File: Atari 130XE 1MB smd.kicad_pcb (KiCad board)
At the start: 2 copper layers, 324 x 204 mm, 366 parts, among them J1 SIO, J10 Mem_on_off, J102 pin, J103 pin, J2 Video, J201 Diagnostic, J202 Diag, J210 Diag, J24 Cartridge, J4 Expansion, J5 Joystick_Port, J50 Test_signal, J500 Basic_sel, J501 TPP_sel, J51 To_GND, J6 Joystick_Port, J7 Power, J8 Keyboard, Q1 2N3904, Q10 PN2222A, Q101 BC849, Q11 PN2222A, Q2 2N3904, Q3 2N3904, Q4 2N3906, Q6 2N3904, SW1 Switch_power_on, U10 DRAM_4464, U100 74LS157, U101 74LS74, U102 74HC02, U103 74HC02, U104 74LS157, U105 74HC74, U17 GTIA, U18 74LS08, U19 LM555, U2 74LS138, U20 4050, U21 74LS74, U22 POKEY, U23 PIA, U24 CD4051B, U25 CD4051B, U3 MMU, U4 27C010, U40 GAL20V8_DIP, U41 74LS157, U42 74LS175, U43 DRAM_1MB_4bit, U44 DRAM_1MB_4bit, U5 27C010, U6 Freddie, U7 Antic, U8 Sally, U9 DRAM_4464, Y1 Crystal, Y2 4,43 MHz

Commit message: ROM refactoring
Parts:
- removed J102, J103: pin, Connector_PinHeader_2.00mm:PinHeader_1x01_P2.00mm_Vertical
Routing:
- net A16_sel: track 0.00 -> 197.3 mm, vias 0 -> 2
- net A15_sel: track 0.00 -> 189.5 mm, vias 0 -> 2
- net A14_sel: track 0.00 -> 131.5 mm, vias 0 -> 2
- net Net-(J500-Pad7): track 2.54 -> 109.7 mm
- net Net-(D101-Pad1): track 11.8 -> 101.8 mm, vias 0 -> 1
- net Net-(J501-Pad3): track 0.00 -> 87.9 mm, vias 0 -> 1
- net D2: track 614.8 -> 574.3 mm
- net D1: track 600.0 -> 561.3 mm
- net D0: track 587.0 -> 549.1 mm
- net +5VA: track 2190.1 -> 2210.8 mm
- net Net-(C44-Pad1): track 19.6 -> 12.1 mm
- net Net-(C203-Pad1): track 28.9 -> 21.9 mm
- net Net-(C45-Pad1): track 22.4 -> 16.8 mm
- net PB1: track 298.6 -> 293.9 mm
- net PB3: track 334.8 -> 330.7 mm
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
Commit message: SMD continue
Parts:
- C204, C51: footprint Atari:C_Axial_L5.1mm_D2.5mm_P12.50mm_Horizontal -> Capacitor_SMD:C_1206_3216Metric_Pad1.42x1.75mm_HandSolder
- D1000: footprint Diode_THT:D_DO-41_SOD81_P12.70mm_Horizontal -> Diode_SMD:D_MELF_Handsoldering
- FB31, L32, L5, L6: footprint Atari:L_Axial_L7.0mm_D3.3mm_P12.50mm_Horizontal_Fastron_MICC -> Inductor_SMD:L_1812_4532Metric_Pad1.30x3.40mm_HandSolder
- R201, R202, R203, R41, R42, R43, R44, R45: footprint Atari:R_Axial_DIN0207_L3.6mm_D2.2mm_P10.16mm_Horizontal -> Resistor_SMD:R_1206_3216Metric_Pad1.42x1.75mm_HandSolder
- moved C204 44.9 mm to (135.5, 148.2), turned to 180 degrees
- moved L32 25.4 mm to (158.0, 153.0), turned to 90 degrees
- moved R201 24.6 mm to (152.5, 146.0), turned to 90 degrees
- moved R203 11.3 mm to (154.9, 146.0)
- moved R45 10.9 mm to (161.2, 146.0)
- moved R42 10.9 mm to (163.5, 146.0)
- moved R41 10.9 mm to (170.4, 146.0)
- moved R44 10.9 mm to (168.1, 146.0)
- moved R43 10.9 mm to (165.8, 146.0)
- moved L6 10.6 mm to (158.0, 146.6)
- moved R202 8.14 mm to (143.4, 148.3), turned to 270 degrees
- moved L5 7.06 mm to (148.8, 148.9), turned to 270 degrees
- moved Q2 6.65 mm to (137.8, 151.7), turned to 180 degrees
- moved FB31 6.25 mm to (140.9, 141.3)
- moved D1000 3.53 mm to (140.5, 149.9), turned to 270 degrees
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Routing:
- net A16_sel: track 197.3 -> 610.2 mm, vias 2 -> 3
- net A14_sel: track 131.5 -> 363.2 mm, vias 2 -> 5
- net Net-(D101-Pad1): track 101.8 -> 305.4 mm, vias 1 -> 2
- net Net-(J501-Pad3): track 87.9 -> 290.7 mm, vias 1 -> 2
- net Net-(J500-Pad7): track 109.7 -> 311.0 mm, vias 1 -> 2
- net A15_sel: track 189.5 -> 390.2 mm, vias 2 -> 4
- net +5VA: track 2210.8 -> 2317.6 mm, vias 51 -> 53
- net GND: track 1692.3 -> 1759.3 mm, vias 72 -> 97
- net COLOR: track 56.2 -> 87.7 mm
- net Net-(L32-Pad2): track 30.8 -> 5.67 mm
- net Net-(R42-Pad2): track 79.5 -> 100.3 mm
- net +5C: track 165.4 -> 148.6 mm, vias 8 -> 7
- net RD4: track 220.5 -> 204.7 mm
- net Net-(U2-Pad4): track 119.7 -> 133.1 mm
- net Net-(Q2-Pad2): track 12.5 -> 21.3 mm, vias 0 -> 1
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
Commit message: SMD continue
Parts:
- C31, C44, C45, C46, C47, C48: footprint Atari:C_Axial_L5.1mm_D2.5mm_P12.50mm_Horizontal -> Capacitor_SMD:C_1206_3216Metric_Pad1.42x1.75mm_HandSolder
- D2, D3, D4: footprint Diode_THT:D_DO-35_SOD27_P12.70mm_Horizontal -> Diode_SMD:D_MiniMELF
- R116, R20, R21, R22, R31, R34, R35, R36, R37, R46, R47, R48, R49, R50, R51: footprint Atari:R_Axial_DIN0207_L3.6mm_D2.2mm_P10.16mm_Horizontal -> Resistor_SMD:R_1206_3216Metric_Pad1.42x1.75mm_HandSolder
- moved C48 31.6 mm to (148.8, 123.5)
- moved J501 20.6 mm to (103.6, 49.6), turned to 0 degrees
- moved R21 20.6 mm to (171.5, 95.3), turned to 270 degrees
- moved R37 15.8 mm to (153.0, 101.3)
- moved R510 14.2 mm to (110.8, 53.4), turned to 0 degrees
- moved R22 13.5 mm to (171.5, 90.2), turned to 90 degrees
- moved R20 12.4 mm to (169.1, 90.2), turned to 270 degrees
- moved R46 11.9 mm to (151.3, 118.1)
- moved R36 11.2 mm to (165.2, 101.3)
- moved R116 11.1 mm to (153.7, 118.1)
- moved D4 11.1 mm to (156.1, 118.3)
- moved C45 9.77 mm to (162.8, 101.3)
- moved C47 9.65 mm to (150.5, 101.3)
- moved C46 9.46 mm to (155.4, 101.3)
- moved J500 8.68 mm to (103.6, 55.9)
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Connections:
- J500 pad 1: A16_sel -> Net-(J500-Pad1)
- J500 pad 3: A15_sel -> A14_sel
- J500 pad 5: A14_sel -> A15_sel
- J500 pad 7: Net-(J500-Pad7) -> A16_sel
- J501 pad 1: Net-(D101-Pad1) -> Net-(J501-Pad1)
- J501 pad 3: Net-(J501-Pad3) -> Net-(D101-Pad1)
- R506 pad 2: Net-(J500-Pad7) -> Net-(J500-Pad1)
- R510 pad 1: Net-(J501-Pad3) -> Net-(J501-Pad1)
- U100 pad 1: Net-(J500-Pad7) -> Net-(J500-Pad1)
- U104 pad 1: Net-(J501-Pad3) -> Net-(J501-Pad1)
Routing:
- net Net-(J500-Pad1): track 0.00 -> 403.5 mm, vias 0 -> 2
- net Net-(J501-Pad1): track 0.00 -> 388.6 mm, vias 0 -> 2
- net Net-(J500-Pad7): track 311.0 -> 0.00 mm, vias 2 -> 0
- net Net-(J501-Pad3): track 290.7 -> 0.00 mm, vias 2 -> 0
- net Net-(D101-Pad1): track 305.4 -> 394.3 mm
- net A14_sel: track 363.2 -> 452.1 mm
- net A15_sel: track 390.2 -> 477.4 mm
- net Net-(Q3-Pad3): track 44.4 -> 5.64 mm
- net COMPOSITE_A: track 47.4 -> 20.9 mm, vias 1 -> 0
- net +5VA: track 2317.6 -> 2343.0 mm, vias 53 -> 57
- net A16_sel: track 610.2 -> 586.3 mm
- net Net-(C48-Pad2): track 148.7 -> 125.9 mm
- net Net-(C47-Pad2): track 59.6 -> 37.3 mm, vias 1 -> 2
- net Net-(Q3-Pad2): track 81.9 -> 66.9 mm, vias 1 -> 0
- net RNMI: track 23.9 -> 37.2 mm, vias 0 -> 1
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
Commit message: Almost finished
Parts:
- C30, C43: footprint Atari:C_Axial_L5.1mm_D2.5mm_P12.50mm_Horizontal -> Capacitor_SMD:C_1206_3216Metric_Pad1.42x1.75mm_HandSolder
- FB9: footprint Atari:L_Axial_L7.0mm_D3.3mm_P12.50mm_Horizontal_Fastron_MICC -> Inductor_SMD:L_1812_4532Metric_Pad1.30x3.40mm_HandSolder
- R12, R204, R52, R53, R74: footprint Atari:R_Axial_DIN0207_L3.6mm_D2.2mm_P10.16mm_Horizontal -> Resistor_SMD:R_1206_3216Metric_Pad1.42x1.75mm_HandSolder
- moved Q11 40.7 mm to (155.4, 85.5)
- moved C160 40.7 mm to (159.6, 83.2)
- moved Q10 40.7 mm to (155.3, 79.3)
- moved R160 40.7 mm to (159.6, 78.5)
- moved R161 40.7 mm to (159.6, 80.8)
- moved R162 40.7 mm to (159.6, 87.9)
- moved R163 40.7 mm to (159.6, 85.5)
- moved R12 35.6 mm to (314.3, 154.5), turned to 0 degrees
- moved R74 29.1 mm to (314.3, 152.1), turned to 0 degrees
- moved C30 20.8 mm to (210.3, 133.2)
- moved Q3 14.2 mm to (134.6, 82.2)
- moved FB9 13.0 mm to (147.8, 85.2)
- moved C43 11.8 mm to (283.7, 139.2), turned to 270 degrees
- moved R53 10.4 mm to (142.0, 85.8)
- moved R204 9.57 mm to (144.5, 85.8)
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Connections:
- R161 pad 2: COMPOSITE_A -> COMPOSITE
- R162 pad 1: COMPOSITE_A -> COMPOSITE
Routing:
- net +5VA: track 2343.0 -> 2401.4 mm, vias 57 -> 55
- net Net-(R74-Pad2): track 3.76 -> 61.6 mm, vias 0 -> 4
- net GND: track 1765.3 -> 1822.3 mm, vias 98 -> 100
- net E3: track 18.1 -> 71.0 mm, vias 1 -> 5
- net COMPOSITE: track 4.65 -> 48.3 mm, vias 0 -> 1
- net Net-(Q3-Pad3): track 5.64 -> 40.5 mm, vias 0 -> 3
- net COMPOSITE_A: track 20.9 -> 0.00 mm
- net COLOR: track 83.5 -> 100.2 mm, vias 0 -> 1
- net MONO_MOD: track 34.5 -> 25.3 mm
- net CHROMA: track 120.6 -> 114.6 mm
- net O0: track 195.5 -> 190.1 mm
- net AUDIO: track 106.6 -> 101.4 mm
- net MONO: track 35.7 -> 31.1 mm, vias 0 -> 1
- net Net-(Q3-Pad2): track 66.9 -> 62.7 mm, vias 0 -> 1
- net +5C: track 148.6 -> 145.1 mm
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
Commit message: gerber
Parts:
- R30: footprint Atari:R_Axial_DIN0207_L3.6mm_D2.2mm_P10.16mm_Horizontal -> Resistor_SMD:R_1206_3216Metric_Pad1.42x1.75mm_HandSolder
- moved R30 26.2 mm to (104.5, 199.8), turned to 180 degrees
- moved R24 1.36 mm to (104.5, 195.1)
- moved R25 1.36 mm to (104.5, 192.8)
- moved R501 1.36 mm to (104.5, 188.1)
- moved R87 1.36 mm to (104.5, 185.8)
- moved R88 1.36 mm to (104.5, 197.5)
- moved R23 1.36 mm to (104.5, 190.5)
- moved R85 1.36 mm to (104.5, 183.5)
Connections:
- U20 pad 16: (no net) -> +5VA
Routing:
- net +5VA: track 2401.4 -> 2462.7 mm, vias 55 -> 58
- net EXTSEL: track 258.0 -> 282.9 mm, vias 8 -> 11
- net IRQ: track 217.2 -> 212.0 mm
- net PB7: track 319.8 -> 314.6 mm
- net RST: track 609.1 -> 612.4 mm, vias 11 -> 12
- net A13: track 365.9 -> 362.6 mm
- net Net-(Q6-Pad3): track 89.5 -> 87.1 mm
- net PB5: track 251.0 -> 248.8 mm
- net BASIC: track 156.2 -> 153.9 mm
- net A12: track 443.2 -> 441.0 mm
- net A14_sel: track 452.1 -> 454.4 mm
- net Net-(R127-Pad2): track 36.5 -> 34.9 mm
- net PB4: track 263.2 -> 261.7 mm
- net PB3: track 333.6 -> 332.2 mm
- net PB6: track 304.7 -> 303.4 mm
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
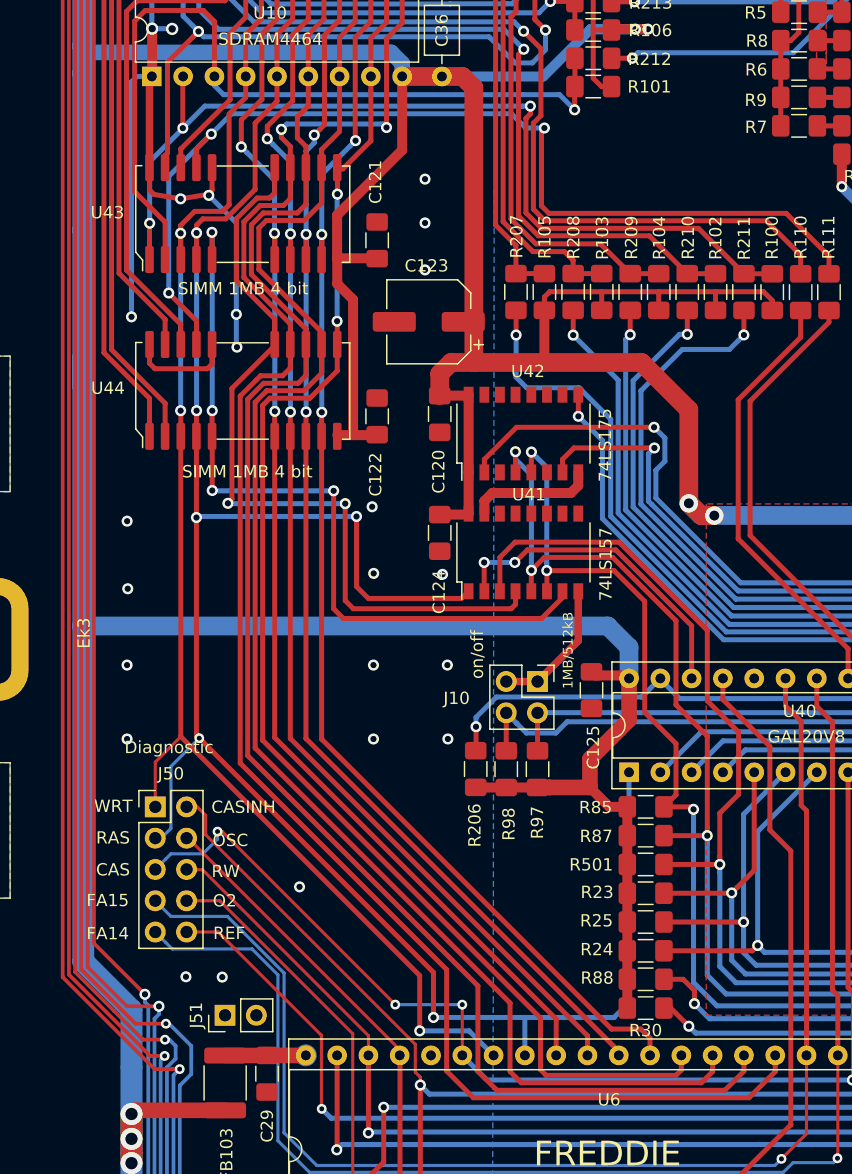
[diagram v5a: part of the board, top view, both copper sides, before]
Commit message: add 74ls04
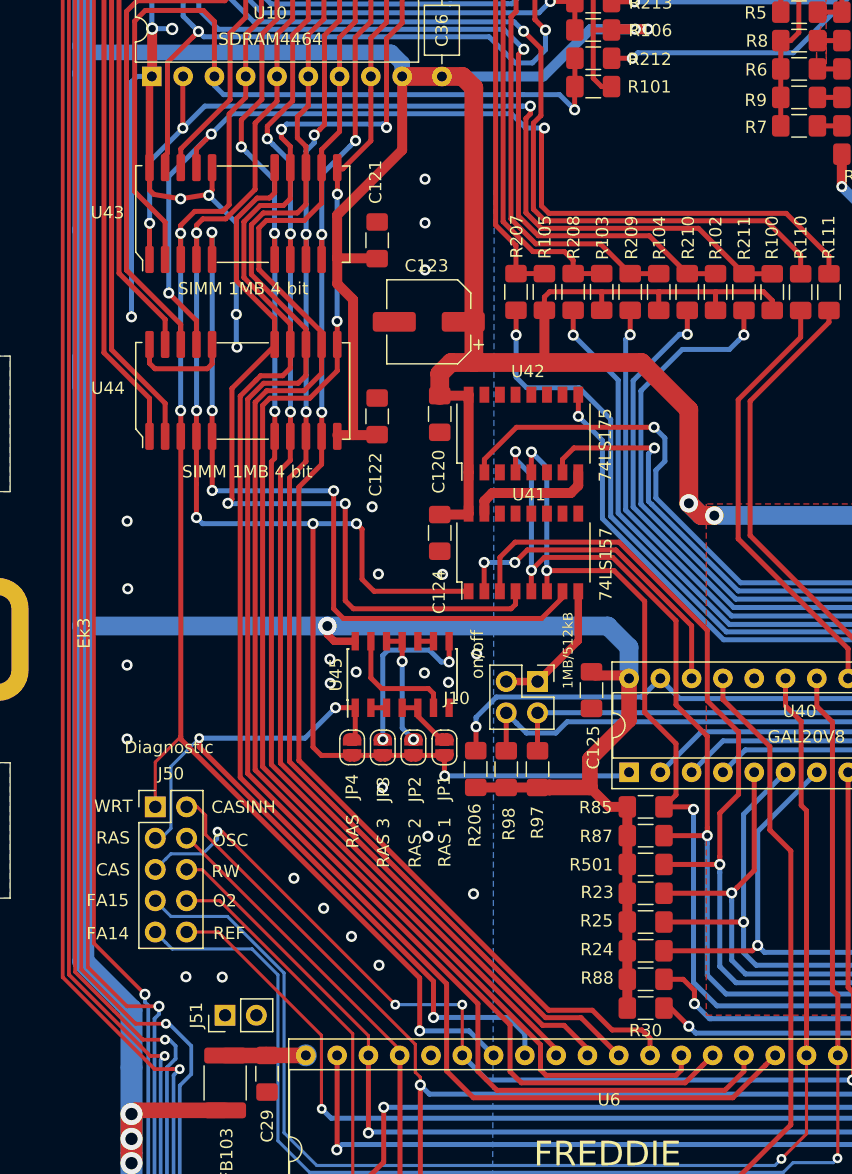
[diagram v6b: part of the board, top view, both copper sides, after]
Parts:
- added JP1: SolderJumper_2_Open, Jumper:SolderJumper-2_P1.3mm_Open_RoundedPad1.0x1.5mm, F.Cu at (88.1, 178.6)
- added JP2: SolderJumper_2_Open, Jumper:SolderJumper-2_P1.3mm_Open_RoundedPad1.0x1.5mm, F.Cu at (85.6, 178.6)
- added JP3: SolderJumper_2_Open, Jumper:SolderJumper-2_P1.3mm_Open_RoundedPad1.0x1.5mm, F.Cu at (83.1, 178.6)
- added JP4: SolderJumper_2_Open, Jumper:SolderJumper-2_P1.3mm_Open_RoundedPad1.0x1.5mm, F.Cu at (80.6, 178.6)
- added U45: 74HC04, Package_SO:SOIC-14_3.9x8.7mm_P1.27mm, F.Cu at (84.7, 172.7)
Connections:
- U10 pad 5: RAS -> RAS_out
- U40 pad 1: RAS -> RAS_out
- U41 pad 1: RAS -> RAS_out
- U43 pad 4: RAS -> RAS_out
- U44 pad 4: RAS -> RAS_out
- U9 pad 5: RAS -> RAS_out
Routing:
- net RAS_out: track 0.00 -> 128.2 mm, vias 0 -> 6
- net RAS: track 180.4 -> 66.5 mm, vias 6 -> 3
- net Net-(JP3-Pad1): track 0.00 -> 14.5 mm, vias 0 -> 2
- net Net-(U45-Pad13): track 0.00 -> 9.74 mm
- net Net-(JP2-Pad1): track 0.00 -> 9.62 mm, vias 0 -> 2
- net Net-(JP1-Pad1): track 0.00 -> 4.89 mm
- net RA3: track 116.9 -> 120.5 mm
- net +5VA: track 2462.7 -> 2465.8 mm, vias 58 -> 59
- net RA2: track 114.4 -> 117.2 mm
- net RA1: track 114.9 -> 116.6 mm
- net Net-(U45-Pad2): track 0.00 -> 1.27 mm
- net Net-(U45-Pad10): track 0.00 -> 1.27 mm
- net RA7: track 155.3 -> 154.5 mm
- net RA5: track 132.2 -> 131.5 mm
- net GND: vias 156 -> 164
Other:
- board text added: "RAS 1"
- board text added: "RAS 2"
- board text added: "RAS 3"
